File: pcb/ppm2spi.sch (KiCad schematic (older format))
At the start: 45 parts, among them IC1 ATMEGA328-A, K1 CONN_3, P1 CONN_5, P2 CONN_6, P3 CONN_3X2, P4 CONN_9, P5 CONN_2, P6 CONN_4, P7 CONN_2, SW1 SW_PUSH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

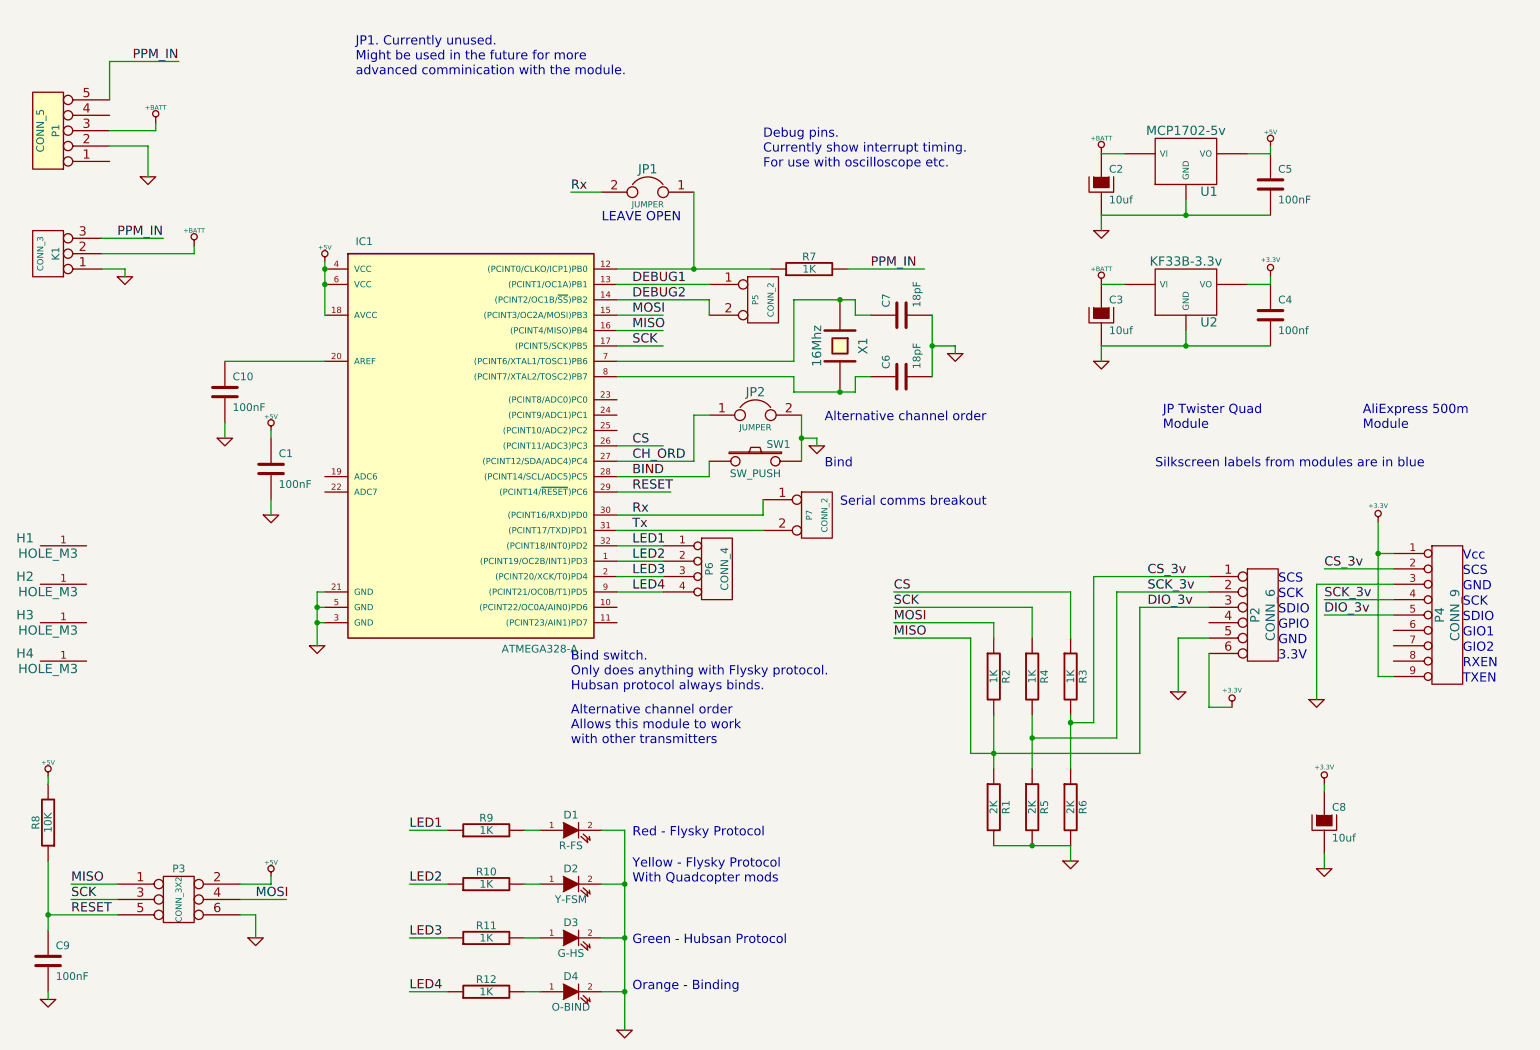
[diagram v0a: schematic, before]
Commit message: Final PCB update to include BAT54S protection diode on PPM input.
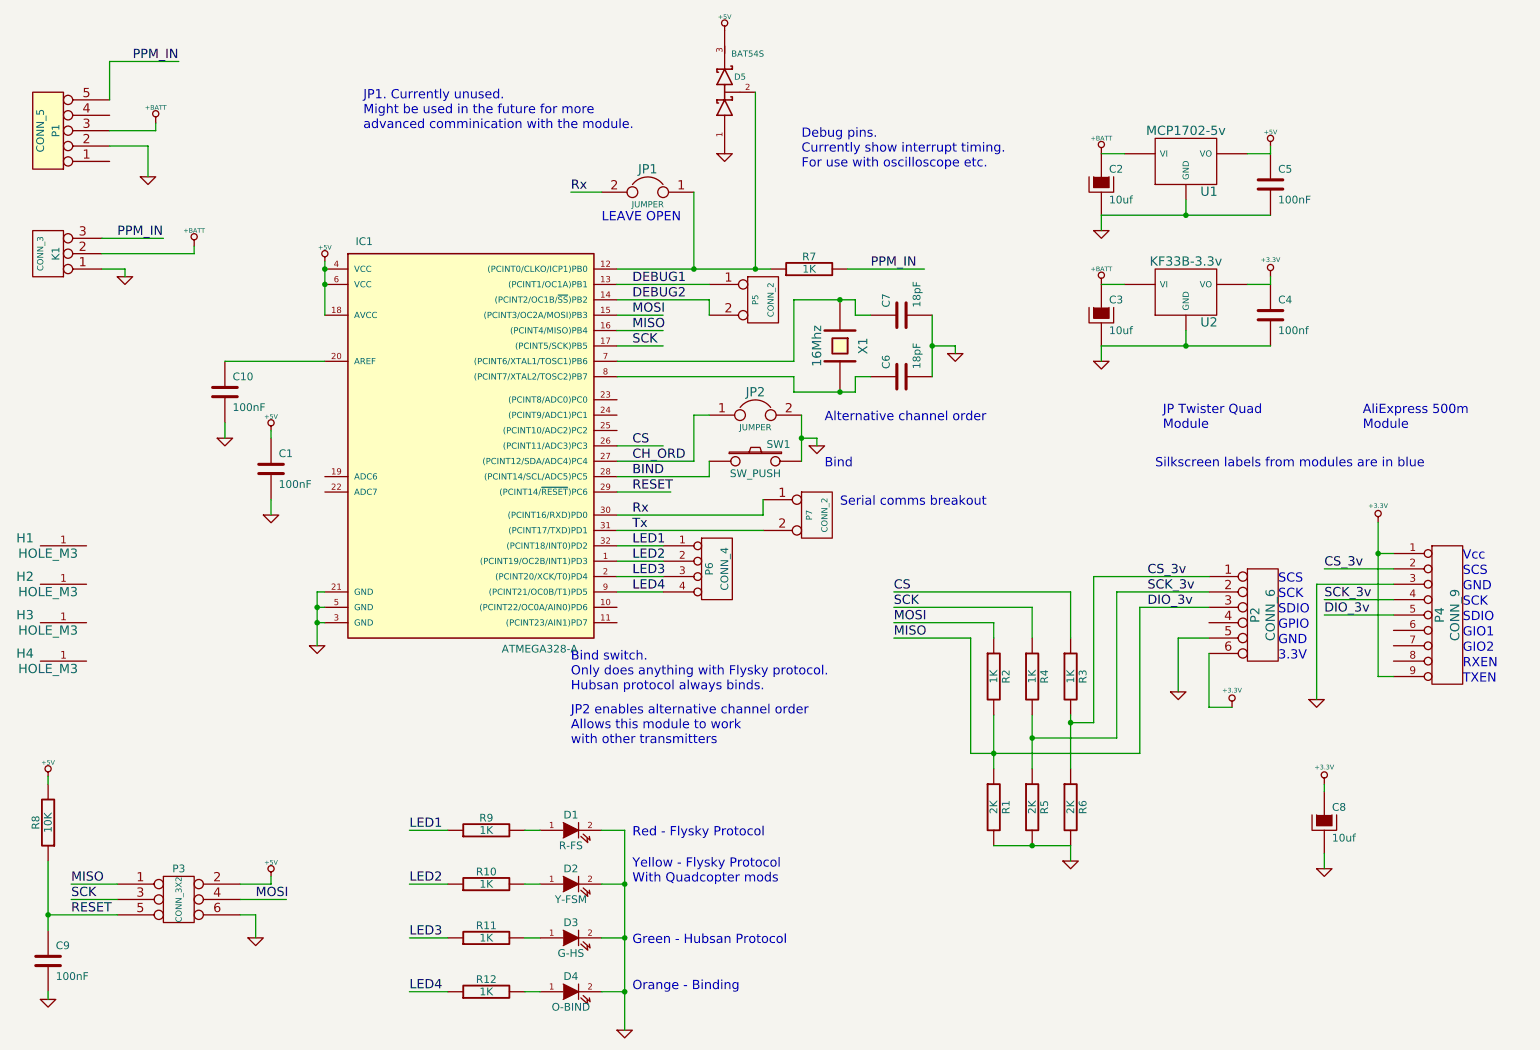
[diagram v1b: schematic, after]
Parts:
- added D5: BAT54S, ~, symbol DOUBLE_SCHOTTKY
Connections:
- wire segments 132 -> 133
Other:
- note added: "JP2 enables alternative channel order\nAllows this module to work\nwith other transmitters"
- note removed: "Alternative channel order\nAllows this module to work\nwith other transmitters"
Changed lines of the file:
@@
-EESchema Schematic File Version 2  date 25/05/2013 20:14:35
+EESchema Schematic File Version 2  date 27/05/2013 10:33:13
 LIBS:power
 LIBS:device
@@
 Sheet 1 1
 Title "ppm2spi Convertor"
-Date "25 may 2013"
+Date "27 may 2013"
 Rev "0.1"
 Comp "Copyright Cameron Weeks <th9xer@gmail.com>"
@@
 Text Notes 4600 5050 0    60   ~ 0
 Bind switch.\nOnly does anything with Flysky protocol.\nHubsan protocol always binds.
-Text Notes 5850 1650 0    60   ~ 0
+Text Notes 6100 1650 0    60   ~ 0
 Debug pins.\nCurrently show interrupt timing.\nFor use with oscilloscope etc.
 $Comp
@@
 Text Notes 4800 2000 0    60   ~ 0
 LEAVE OPEN
-Text Notes 3200 1050 0    60   ~ 0
+Text Notes 3250 1400 0    60   ~ 0
 JP1. Currently unused.\nMight be used in the future for more\nadvanced comminication with the module.
 Text Notes 5000 6700 0    60   ~ 0
@@
 Alternative channel order
 Text Notes 4600 5400 0    60   ~ 0
-Alternative channel order\nAllows this module to work\nwith other transmitters
+JP2 enables alternative channel order\nAllows this module to work\nwith other transmitters
 Text Label 5000 3900 0    60   ~ 0
 Rx
@@
 Wire Wire Line
 	1700 2300 1700 2350
+$Comp
+L DOUBLE_SCHOTTKY D5
+U 1 1 51A32958
+P 5600 1150
+F 0 "D5" V 5700 1050 40  0000 C CNN
+F 1 "BAT54S" V 5850 1000 40  0000 C CNN
+F 2 "~" H 5600 1150 60  0000 C CNN
+F 3 "~" H 5600 1150 60  0000 C CNN
+	1    5600 1150
+	0    -1   -1   0
+$EndComp
+$Comp
+L GND #PWR030
+U 1 1 51A32972
+P 5600 1550
+F 0 "#PWR030" H 5600 1550 30  0001 C CNN
+F 1 "GND" H 5600 1480 30  0001 C CNN
+F 2 "" H 5600 1550 60  0001 C CNN
+F 3 "" H 5600 1550 60  0001 C CNN
+	1    5600 1550
+	1    0    0    -1
+$EndComp
+$Comp
+L +5V #PWR031
+U 1 1 51A32978
+P 5600 750
+F 0 "#PWR031" H 5600 840 20  0001 C CNN
+F 1 "+5V" H 5600 840 30  0000 C CNN
+F 2 "" H 5600 750 60  0001 C CNN
+F 3 "" H 5600 750 60  0001 C CNN
+	1    5600 750
+	1    0    0    -1
+$EndComp
+Wire Wire Line
+	5800 1150 5800 2300
+Connection ~ 5800 2300
 $EndSCHEMATC

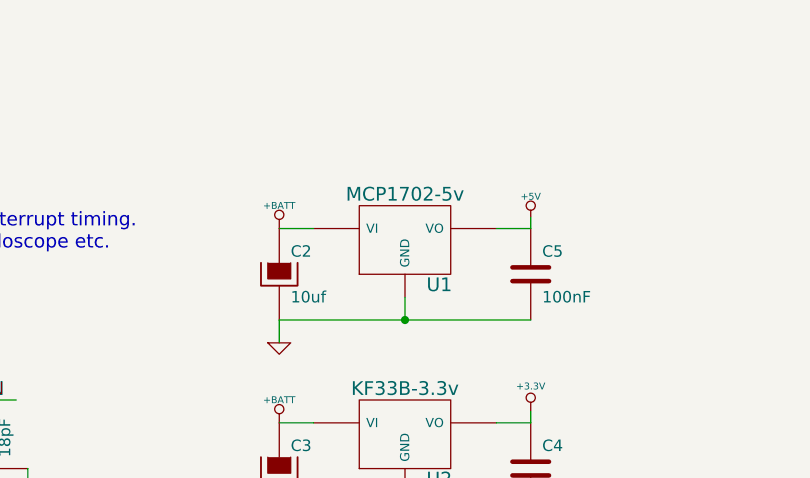
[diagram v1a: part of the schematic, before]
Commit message: Upgraded the 5v reg. The previous post looks like it was nothing to do with the 5v reg but I upgraded it anyway.
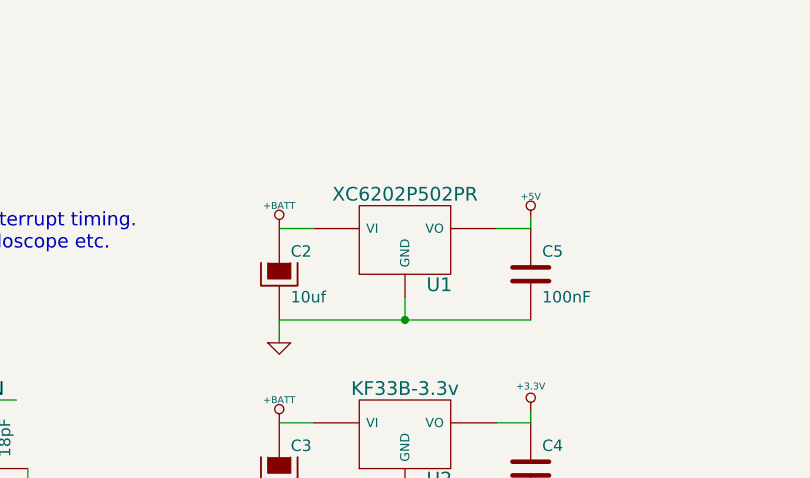
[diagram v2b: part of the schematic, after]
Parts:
- U1: value MCP1702-5v -> XC6202P502PR
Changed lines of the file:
@@
-EESchema Schematic File Version 2  date 27/05/2013 10:33:13
+EESchema Schematic File Version 2  date 28/05/2013 10:33:40
 LIBS:power
 LIBS:device
@@
 Sheet 1 1
 Title "ppm2spi Convertor"
-Date "27 may 2013"
+Date "28 may 2013"
 Rev "0.1"
 Comp "Copyright Cameron Weeks <th9xer@gmail.com>"
@@
 P 8600 1600
 F 0 "U1" H 8750 1404 60  0000 C CNN
-F 1 "MCP1702-5v" H 8600 1800 60  0000 C CNN
+F 1 "XC6202P502PR" H 8600 1800 60  0000 C CNN
 F 2 "" H 8600 1600 60  0001 C CNN
 F 3 "" H 8600 1600 60  0001 C CNN

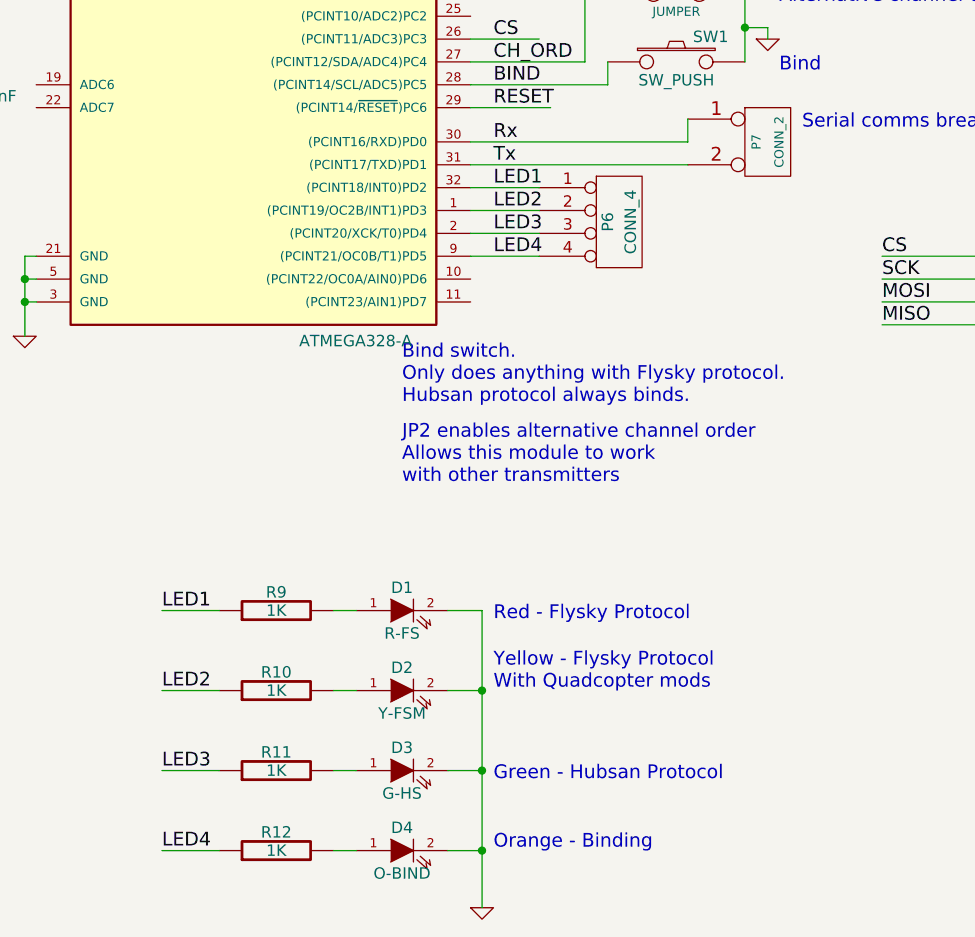
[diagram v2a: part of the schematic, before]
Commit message: LED colour mix up corrected. Orange was right, the rest not so.
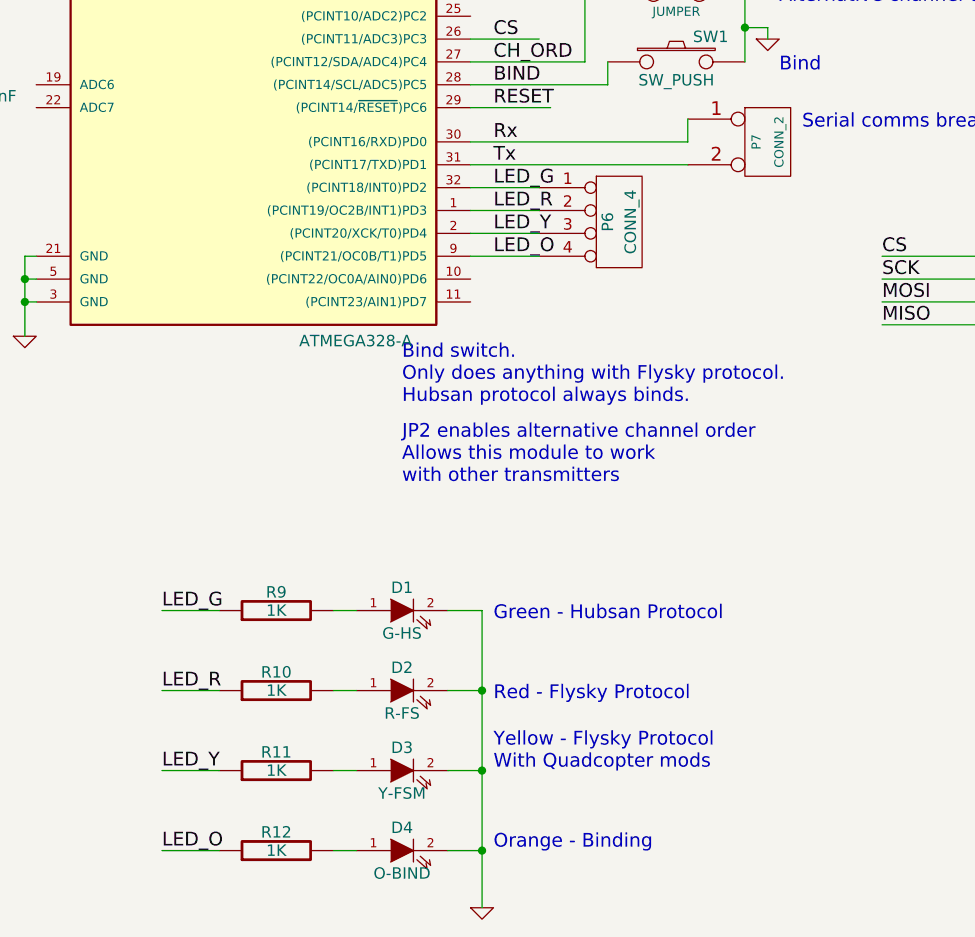
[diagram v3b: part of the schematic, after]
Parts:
- renumbered D3 to D1, D1 to D2, D2 to D3
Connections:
- net labels added: LED_G, LED_O, LED_R, LED_Y
- net labels removed: LED1, LED2, LED3, LED4
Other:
- moved on the sheet: D1, D2, D3
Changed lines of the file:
@@
-EESchema Schematic File Version 2  date 28/05/2013 10:33:40
+EESchema Schematic File Version 2  date 28/05/2013 11:10:31
 LIBS:power
 LIBS:device
@@
 	0    -1   -1   0
 $EndComp
+Text Label 5000 4100 0    60   ~ 0
+LED_G
 Text Label 5000 4300 0    60   ~ 0
-LED3
+LED_Y
 Text Label 5000 4200 0    60   ~ 0
-LED2
-Text Label 5000 4100 0    60   ~ 0
-LED1
+LED_R
 $Comp
 L GND #PWR01
@@
 Text Label 5000 2400 0    60   ~ 0
 DEBUG1
+Text Label 3550 5950 0    60   ~ 0
+LED_G
 Text Label 3550 6650 0    60   ~ 0
-LED3
+LED_Y
 Text Label 3550 6300 0    60   ~ 0
-LED2
-Text Label 3550 5950 0    60   ~ 0
-LED1
+LED_R
 $Comp
 L GND #PWR06
@@
 $EndComp
 $Comp
+L LED D1
+U 1 1 513DD20F
+P 4600 5950
+F 0 "D1" H 4600 6050 50  0000 C CNN
+F 1 "G-HS" H 4600 5850 50  0000 C CNN
+F 2 "" H 4600 5950 60  0001 C CNN
+F 3 "" H 4600 5950 60  0001 C CNN
+	1    4600 5950
+	1    0    0    -1
+$EndComp
+$Comp
 L LED D3
-U 1 1 513DD20F
+U 1 1 513DD20C
 P 4600 6650
 F 0 "D3" H 4600 6750 50  0000 C CNN
-F 1 "G-HS" H 4600 6550 50  0000 C CNN
+F 1 "Y-FSM" H 4600 6550 50  0000 C CNN
 F 2 "" H 4600 6650 60  0001 C CNN
 F 3 "" H 4600 6650 60  0001 C CNN
@@
 $Comp
 L LED D2
-U 1 1 513DD20C
+U 1 1 513DD209
 P 4600 6300
 F 0 "D2" H 4600 6400 50  0000 C CNN
-F 1 "Y-FSM" H 4600 6200 50  0000 C CNN
+F 1 "R-FS" H 4600 6200 50  0000 C CNN
 F 2 "" H 4600 6300 60  0001 C CNN
 F 3 "" H 4600 6300 60  0001 C CNN
 	1    4600 6300
-	1    0    0    -1
-$EndComp
-$Comp
-L LED D1
-U 1 1 513DD209
-P 4600 5950
-F 0 "D1" H 4600 6050 50  0000 C CNN
-F 1 "R-FS" H 4600 5850 50  0000 C CNN
-F 2 "" H 4600 5950 60  0001 C CNN
-F 3 "" H 4600 5950 60  0001 C CNN
-	1    4600 5950
 	1    0    0    -1
 $EndComp
@@
 Text Notes 3250 1400 0    60   ~ 0
 JP1. Currently unused.\nMight be used in the future for more\nadvanced comminication with the module.
-Text Notes 5000 6700 0    60   ~ 0
+Text Notes 5000 6000 0    60   ~ 0
 Green - Hubsan Protocol
-Text Notes 5000 6300 0    60   ~ 0
+Text Notes 5000 6650 0    60   ~ 0
 Yellow - Flysky Protocol\nWith Quadcopter mods
-Text Notes 5000 6000 0    60   ~ 0
+Text Notes 5000 6350 0    60   ~ 0
 Red - Flysky Protocol
 $Comp
@@
 	3800 7000 3550 7000
 Text Label 3550 7000 0    60   ~ 0
-LED4
+LED_O
 Text Notes 5000 7000 0    60   ~ 0
 Orange - Binding
 Text Label 5000 4400 0    60   ~ 0
-LED4
+LED_O
 $Comp
 L CONN_4 P6

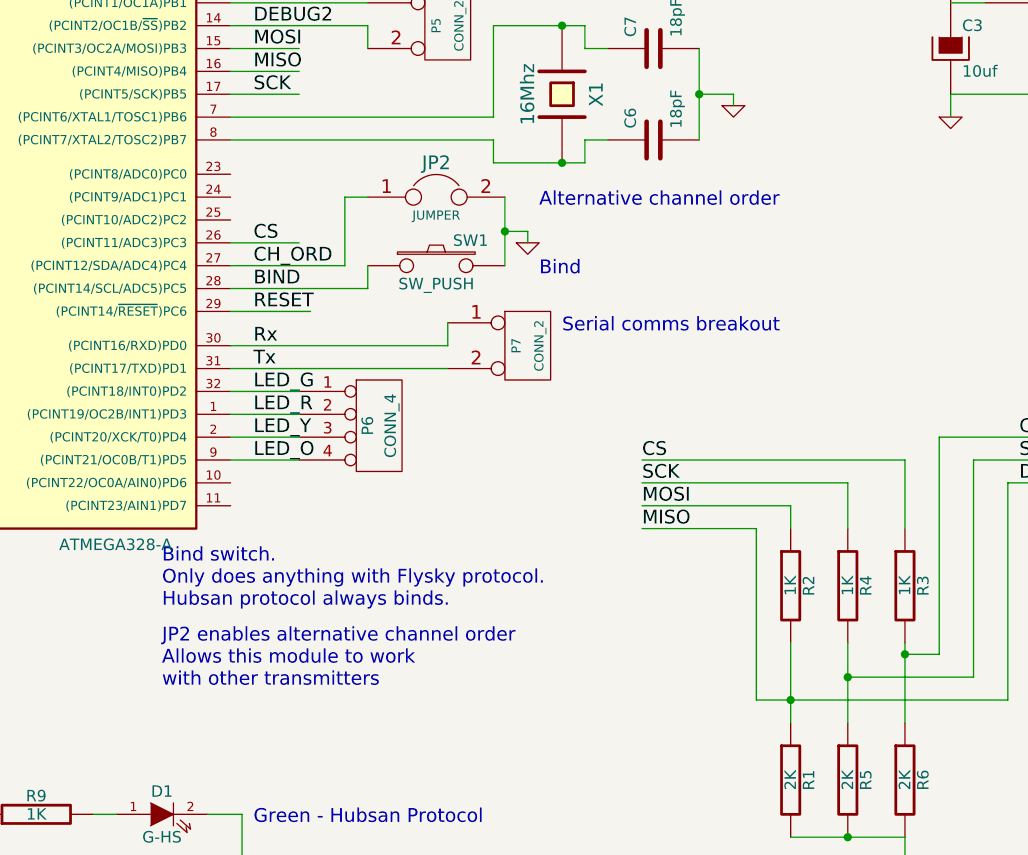
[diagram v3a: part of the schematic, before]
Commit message: Comments on schematic updated, and setup code for channel order pin (does nothing currently).
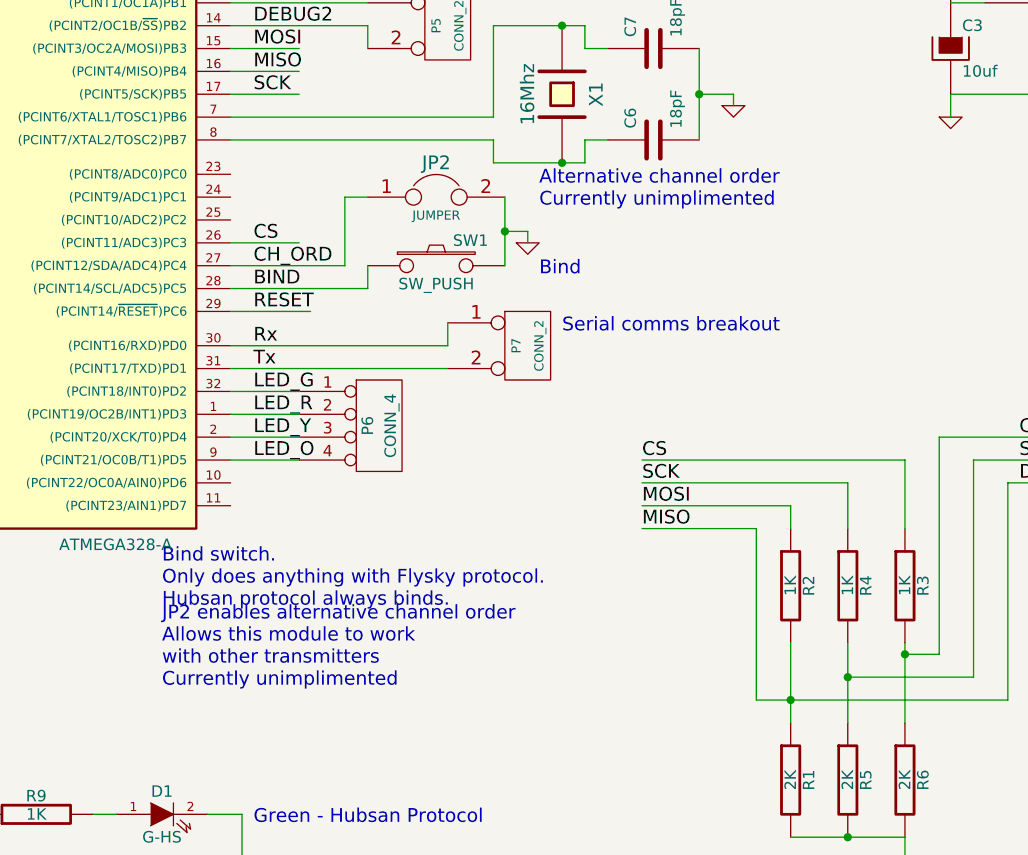
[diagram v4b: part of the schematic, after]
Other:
- note added: "Alternative channel order\nCurrently unimplimented"
- note added: "JP2 enables alternative channel order\nAllows this module to work\nwith other transmitters\nCurrently unimplimented"
- note removed: "Alternative channel order"
- note removed: "JP2 enables alternative channel order\nAllows this module to work\nwith other transmitters"
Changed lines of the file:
@@
-EESchema Schematic File Version 2  date 28/05/2013 11:10:31
+EESchema Schematic File Version 2  date 28/05/2013 11:24:14
 LIBS:power
 LIBS:device
@@
 Bind
 Text Notes 6250 3300 0    60   ~ 0
-Alternative channel order
+Alternative channel order\nCurrently unimplimented
 Text Notes 4600 5400 0    60   ~ 0
-JP2 enables alternative channel order\nAllows this module to work\nwith other transmitters
+JP2 enables alternative channel order\nAllows this module to work\nwith other transmitters\nCurrently unimplimented
 Text Label 5000 3900 0    60   ~ 0
 Rx
